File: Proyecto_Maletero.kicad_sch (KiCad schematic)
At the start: 34 parts, among them J2 Conn_01x02, J3 Conn_01x02, J4 Conn_01x03, J5 Conn_01x02, J7 Conn_01x03, J8 Conn_01x02, J9 Conn_01x02, SW1 SW_Push, SW3 SW_SPST, U1 LT1117-ADJ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

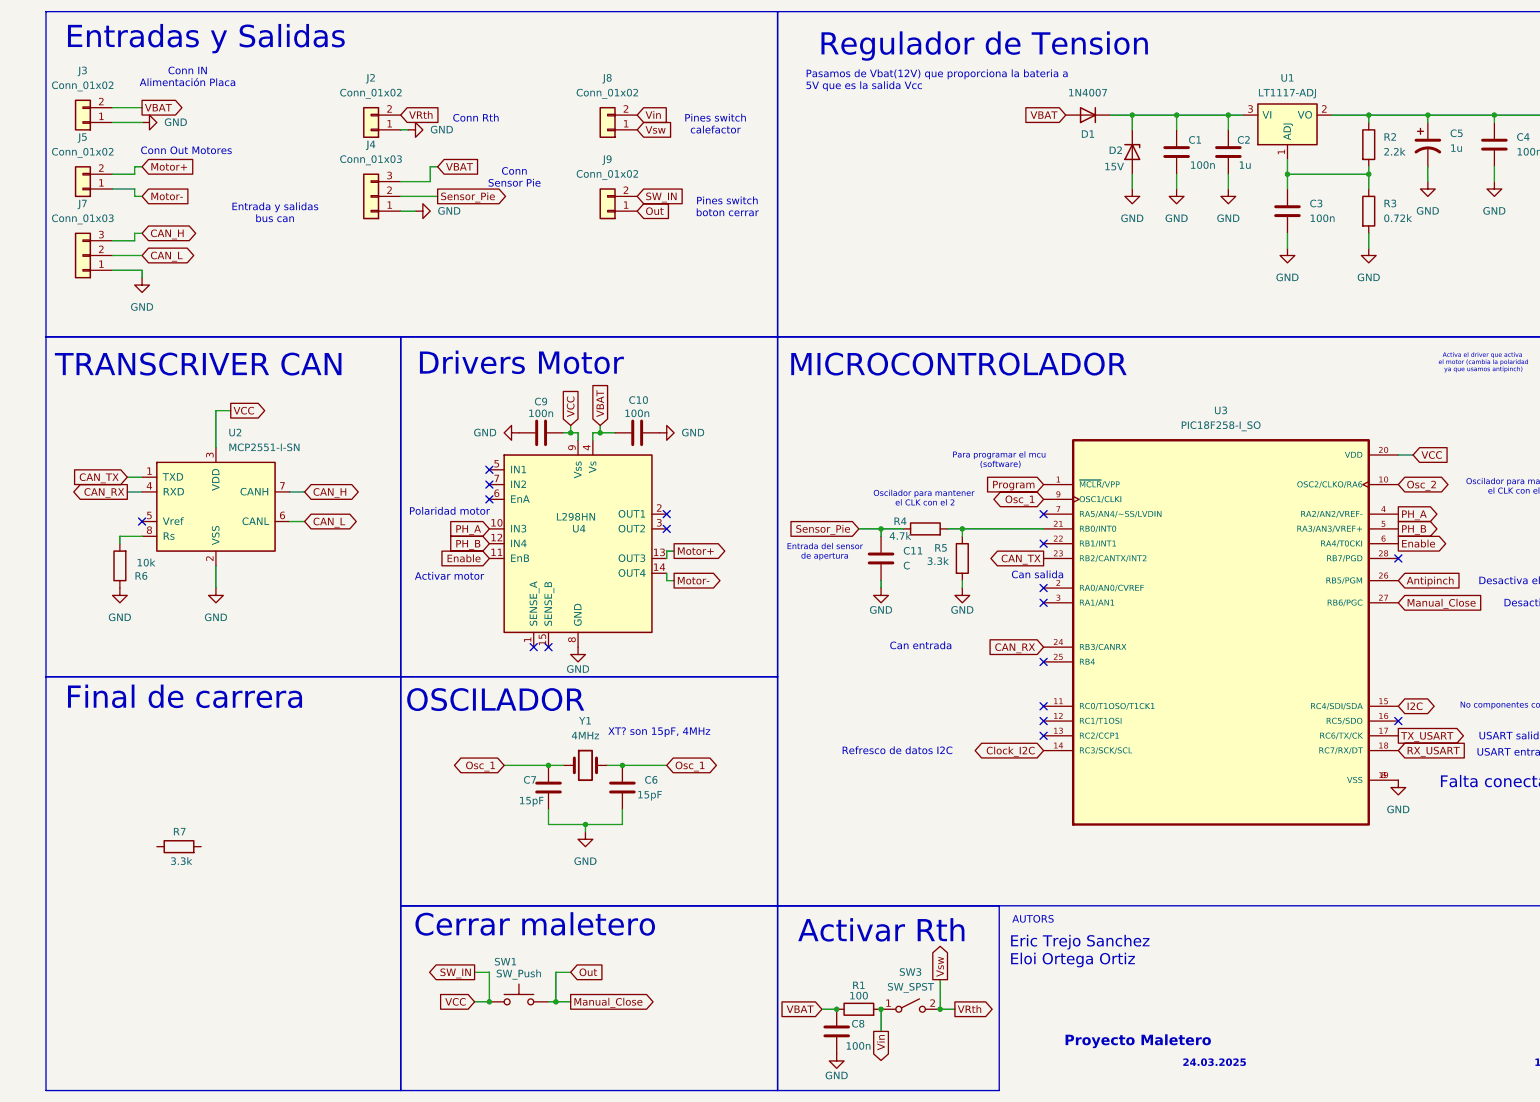
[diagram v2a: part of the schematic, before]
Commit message: Version casi final
Anadiodo, final de carrera, seleccion de pines, y condensadores de desacoplamiento
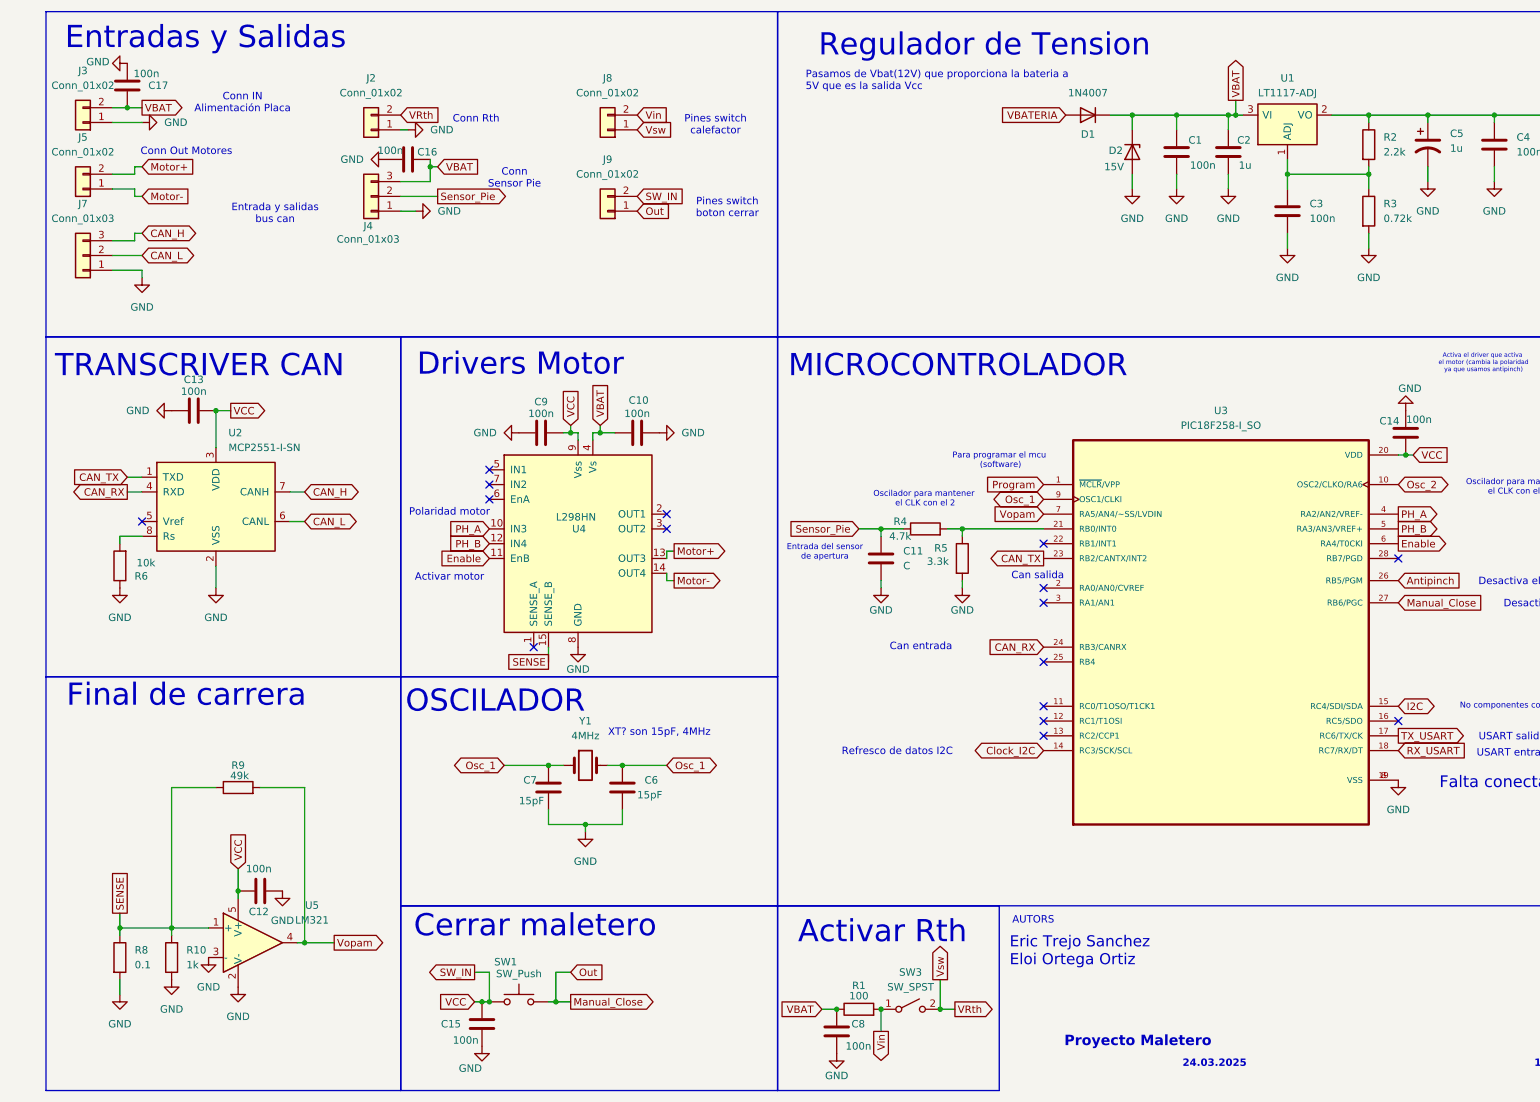
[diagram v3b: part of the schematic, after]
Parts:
- removed R7: 3.3k, symbol Device:R
- added C12, C13, C14, C15, C16, C17: 100n, symbol Device:C
- added R10: 1k, symbol Device:R
- added R8: 0.1, symbol Device:R
- added R9: 49k, symbol Device:R
- added U5: LM321, Package_TO_SOT_SMD:SOT-23-5, symbol Amplifier_Operational:LM321
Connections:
- net GND: now also C12.2, C13.1, C14.1, C15.1, C16.1, C17.1, R10.1, R8.2, U5.2 (V-), U5.3 (-)
- net SW_IN: now also C12.1, C13.2, C14.2, C15.2, U5.5 (V+)
- net VBAT: now also C1.1, C2.1, D1.1 (K), D2.1 (K), U1.3 (VI), C16.2, C17.2; no longer D1.2 (A)
- net SENSE: now reaches U4.15 (SENSE_B)
- net SENSE: now also R10.2, R8.1, R9.1, U5.1 (+)
- net Vopam: now reaches U3.7 (RA5/AN4/~SS/LVDIN)
- net Vopam: now also R9.2, U5.4
- new net VBATERIA: D1.2 (A)
- no-connect marks 18 -> 16

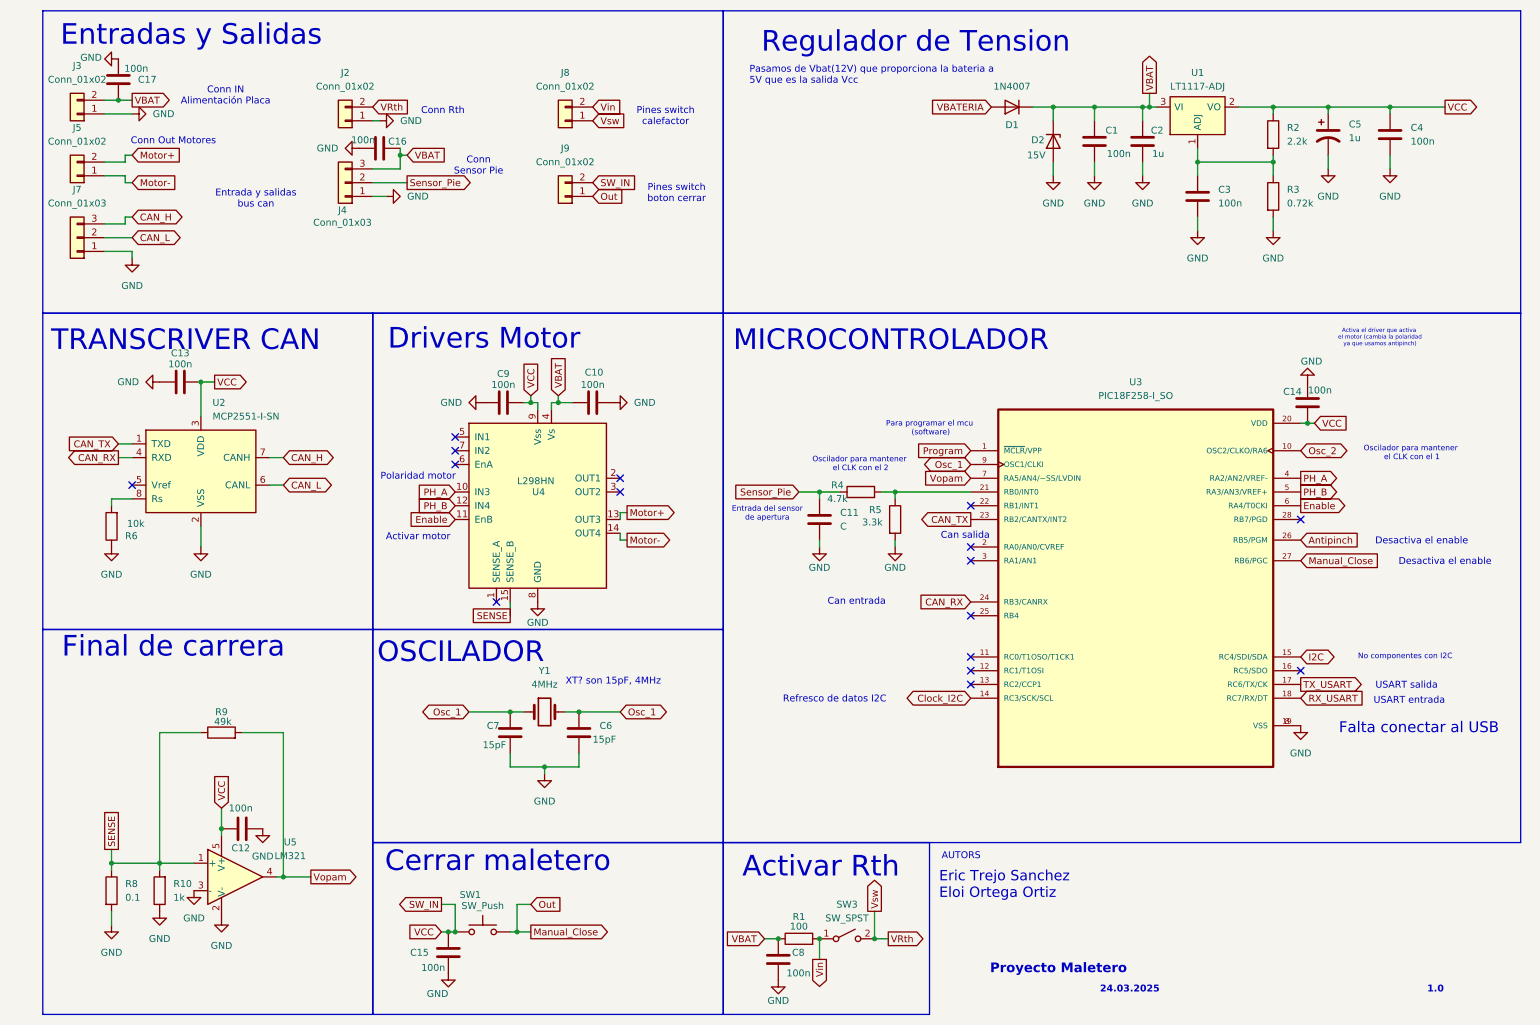
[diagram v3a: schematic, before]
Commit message: Corrección CAN y separación
Hemos puesto una resistencia para los extremos del bus CAN. Tambien hemos separado los tags para que no se vea tan junto
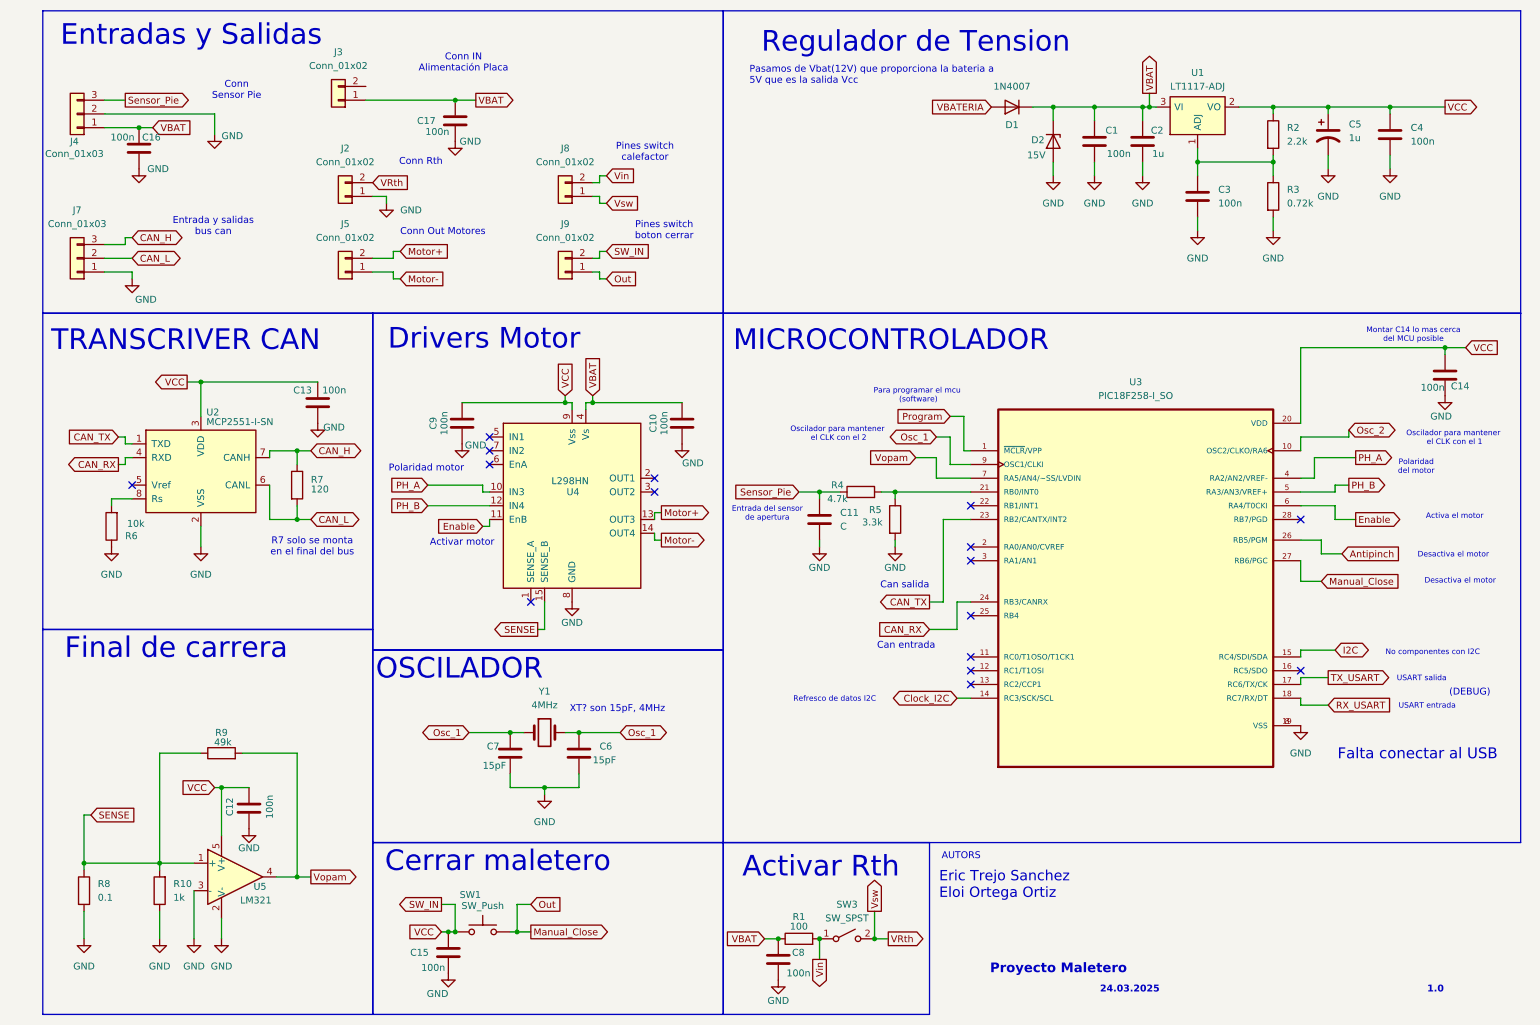
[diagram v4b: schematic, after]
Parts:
- added R7: 120, symbol Device:R
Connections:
- net CAN_H: now also R7.1
- net CAN_L: now also R7.2
- net GND: now also C10.1, J4.2 (Pin_2); no longer C10.2, J3.1 (Pin_1), J4.1 (Pin_1)
- net Sensor_Pie: now also J4.3 (Pin_3); no longer J4.2 (Pin_2)
- net VBAT: now also C10.2, J3.1 (Pin_1), J4.1 (Pin_1); no longer C10.1, J3.2 (Pin_2), J4.3 (Pin_3)
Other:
- note added: "(DEBUG)"
- note added: "Activa el motor"
- note added: "Desactiva el motor"
- note added: "Montar C14 lo mas cerca del MCU posible"
- note added: "Polaridad del motor"
- note added: "R7 solo se monta en el final del bus"
- note removed: "Activa el driver que activa el motor (cambia la polaridad ya que usamos antipinch)"
- note removed: "Desactiva el enable"
- moved on the sheet: C12, C13, C14, C16, C17, C6, C7, C9, J2, J3, J4, J5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

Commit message: Rth menos enano
Hemos expandido Rth
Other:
- note added: "Detector antipinch"
- note added: "Salida al motor"
- moved on the sheet: C15, C8, R1, SW1, SW3

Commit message: Añadir NET list,modificacion de erros,, y regulador
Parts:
- removed C3: 100n, symbol Device:C
- removed R2: 2.2k, symbol Device:R
- removed R3: 0.72k, symbol Device:R
- removed U1: LT1117-ADJ, symbol Regulator_Linear:LT1117-ADJ
- added U1: LM1084-5.0, symbol Regulator_Linear:LM1084-5.0
- D1: value 1N4007 -> RF601BGE2D
- D2: value 15V -> 12V
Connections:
- net GND: now also J3.2 (Pin_2), U1.1 (GND)
- net SW_IN: now also U1.2 (VO)
- net VBAT: now also U1.3 (VI)
- net Antipinch: no longer names the net of U3.26 (RB5/PGM)
- net CAN_H renamed CAN+
- net CAN_L renamed CAN-
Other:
- note added: "1.1"
- note removed: "1.0"
- moved on the sheet: C1, C2, C4, C5, D1, D2

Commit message: Cambio de orden y posición de conn
Tambien he añadido los DE-9, creo que el USART necesita un convertidor o algo asi, igual lo quitamos.
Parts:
- added J1, J6: DE9_Pins, symbol Connector:DE9_Pins
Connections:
- net CAN+: now also J1.7
- net CAN-: now also J1.2
- net GND: now also J1.3
- net RX_USART: now also J6.2
- net TX_USART: now also J6.3
- net VBAT: now also J1.9, J6.9
- no-connect marks 16 -> 21
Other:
- note removed: "Entradas y Salidas"
- moved on the sheet: C1, C10, C11, C12, C13, C14, C15, C16, C17, C2, C4, C5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

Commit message: Correcciones de la version anterior
Falta cambiar los nets múltiples esos
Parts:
- removed J7: Conn_01x03, symbol Connector_Generic:Conn_01x03
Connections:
- net SW_IN: now also J1.9, J6.9
- net VBAT: no longer J1.9, J6.9
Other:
- note added: "Regulador de Tensión"
- note removed: "Entrada y salidas bus can"
- note removed: "Regulador de Tension"
- moved on the sheet: C1, C10, C11, C12, C13, C14, C15, C16, C17, C2, C4, C5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
